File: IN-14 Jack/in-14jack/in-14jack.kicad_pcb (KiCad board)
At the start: 2 copper layers, 24 x 24 mm, 2 parts, among them J1 Conn_01x13_Male, J2 Conn_01x13_Female

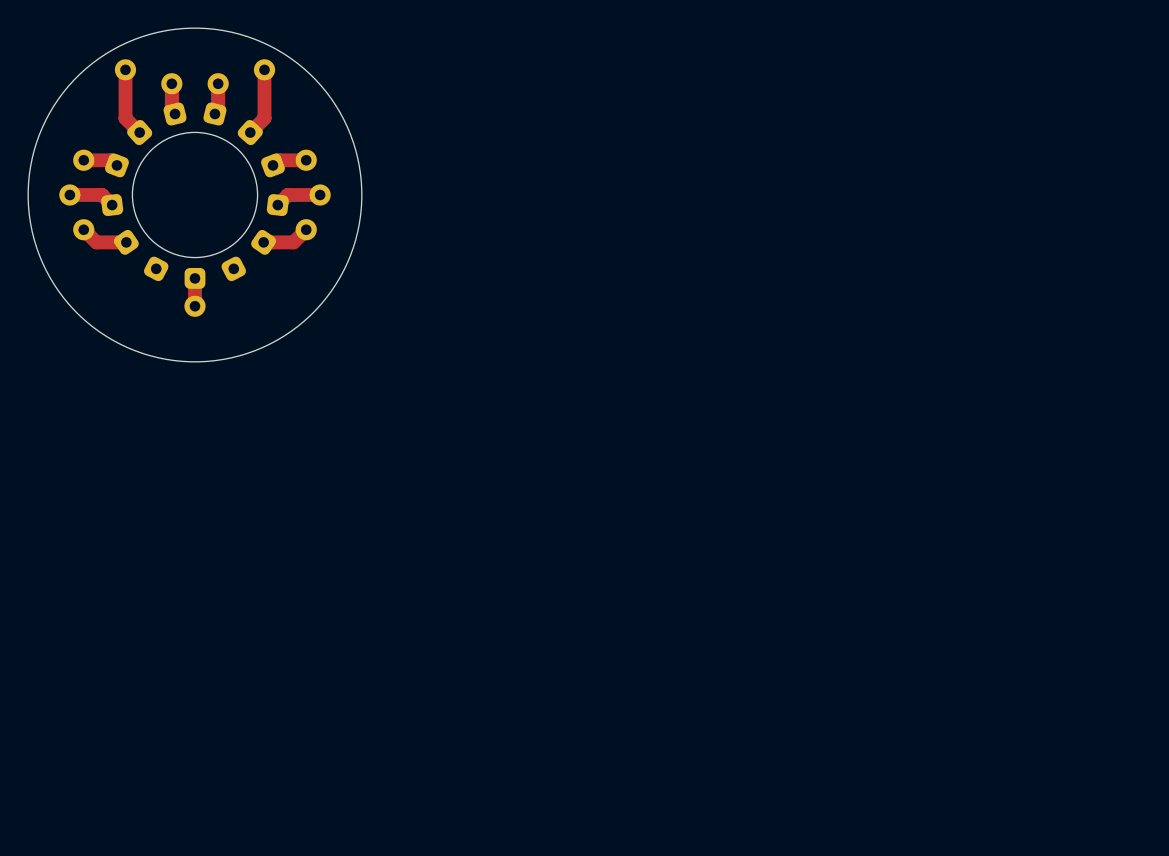
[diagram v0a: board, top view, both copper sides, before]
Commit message: 原理图修改，同步
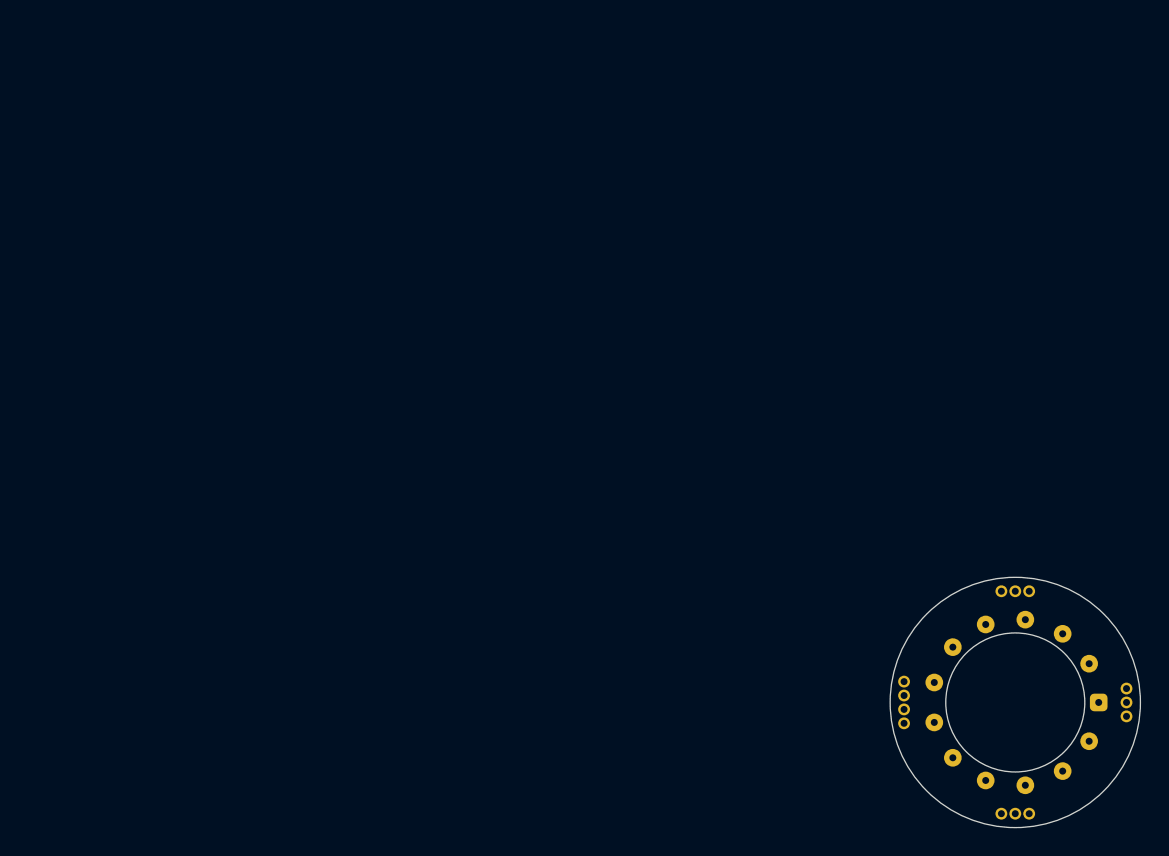
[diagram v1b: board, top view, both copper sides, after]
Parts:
- removed J1: Conn_01x13_Male, HGHardware:NixieTubeJack
- removed J2: Conn_01x13_Female, in-14jack:in-14
- added REF**: pad, in-14jack:pad, F.Cu at (86.0, 68.5)
- added REF**: pad, in-14jack:pad, F.Cu at (94.0, 78.0)
- added REF**: pad, in-14jack:pad, F.Cu at (102.0, 71.0)
- added REF**: pad, in-14jack:pad, F.Cu at (102.0, 69.0)
- added REF**: pad, in-14jack:pad, F.Cu at (102.0, 70.0)
- added REF**: pad, in-14jack:pad, F.Cu at (99.3, 72.8)
- added REF**: pad, in-14jack:pad, F.Cu at (97.4, 74.9)
- added REF**: pad, in-14jack:pad, F.Cu at (94.7, 76.0)
- added REF**: pad, in-14jack:pad, F.Cu at (91.9, 75.6)
- added REF**: pad, in-14jack:pad, F.Cu at (89.5, 74.0)
- added REF**: pad, in-14jack:pad, F.Cu at (88.2, 71.4)
- added REF**: pad, in-14jack:pad, F.Cu at (86.0, 71.5)
- added REF**: pad, in-14jack:pad, F.Cu at (88.2, 68.6)
- added REF**: pad, in-14jack:pad, F.Cu at (89.5, 66.0)
- added REF**: pad, in-14jack:pad, F.Cu at (91.9, 64.4)
- added REF**: pad, in-14jack:pad, F.Cu at (94.7, 64.0)
- added REF**: pad, in-14jack:pad, F.Cu at (97.4, 65.1)
- added REF**: pad, in-14jack:pad, F.Cu at (99.3, 67.2)
- added REF**: pad, in-14jack:pad, F.Cu at (100.0, 70.0)
- added REF**: pad, in-14jack:pad, F.Cu at (86.0, 69.5)
- added REF**: pad, in-14jack:pad, F.Cu at (86.0, 70.5)
- added REF**: pad, in-14jack:pad, F.Cu at (93.0, 62.0)
- added REF**: pad, in-14jack:pad, F.Cu at (95.0, 62.0)
- added REF**: pad, in-14jack:pad, F.Cu at (94.0, 62.0)
- added REF**: pad, in-14jack:pad, F.Cu at (93.0, 78.0)
- added REF**: pad, in-14jack:pad, F.Cu at (95.0, 78.0)
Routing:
- net Net-(J1-Pad6): track 4.93 -> 0.00 mm
- net Net-(J1-Pad9): track 4.93 -> 0.00 mm
- net Net-(J1-Pad12): track 3.44 -> 0.00 mm
- net Net-(J1-Pad3): track 3.44 -> 0.00 mm
- net Net-(J1-Pad4): track 3.34 -> 0.00 mm
- net Net-(J1-Pad11): track 3.34 -> 0.00 mm
- net Net-(J1-Pad10): track 2.54 -> 0.00 mm
- net Net-(J1-Pad5): track 2.54 -> 0.00 mm
- net Net-(J1-Pad8): track 2.27 -> 0.00 mm
- net Net-(J1-Pad7): track 2.27 -> 0.00 mm
- net Net-(J1-Pad1): track 2.00 -> 0.00 mm
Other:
- board size 24 x 24 mm -> 18 x 18 mm
